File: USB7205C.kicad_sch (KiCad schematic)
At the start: 92 parts, among them CN8 W25Q128FVIQ_Connector, U13 25MHz, U19 LX7167ACLD-TR, U20 USB7205C-I_KDX, U31 USB7206C-I_KDX

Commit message: Initial design of USB7205C
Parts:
- removed C207, C209, C210, C211, C212, C74, C75, C76, C77, C78, C79, C80, C81, C82, C83, C86, C87, C88: 100nF, Capacitor_SMD:C_0402_1005Metric, symbol JLCImport:CL05B104KB54PNC
- removed C67, C73: 15pF, Capacitor_SMD:C_0402_1005Metric, symbol JLCImport:0402CG150J500NT
- removed C84: 10uF, Capacitor_SMD:C_0805_2012Metric, symbol JLCImport:CL21A106KAYNNNE
- removed R189, R60: 200k, Resistor_SMD:R_0603_1608Metric, symbol JLCImport:0603WAF2003T5E
- removed R190, R191, R192, R193, R204, R205, R206, R207, R55, R59: 10k, Resistor_SMD:R_0402_1005Metric, symbol JLCImport:0402WGF1002TCE
- removed R217, R218, R219, R220, R221, R222, R223: 100k, Resistor_SMD:R_0402_1005Metric, symbol JLCImport:0402WGF1003TCE
- removed R376, R394: 100k, Resistor_SMD:R_0402_1005Metric, symbol JLCImport:HP02WAF1003TCE
- removed R54: 12k±1%, Resistor_SMD:R_0402_1005Metric, symbol JLCImport:CR0402F12K0Q10Z
- removed TP2: A, TestPoint:TestPoint_Pad_1.0x1.0mm, symbol Connector:TestPoint
- removed U13: 25MHz, JLCImport:25M_10PF_50PPM, symbol JLCImport:25M_10PF_50PPM
- removed U31: USB7206C-I_KDX, JLCImport:USB7206C-I_KDX, symbol JLCImport:USB7206C-I_KDX
- added C199, C214: 15pF, Capacitor_SMD:C_0402_1005Metric, symbol JLCImport:0402CG150J500NT
- added C216, C217, C218, C219, C221, C222, C304, C321, C322, C323, C324, C325, C326, C327, C328, C329, C330: 100nF, Capacitor_SMD:C_0402_1005Metric, symbol JLCImport:CL05B104KB54PNC
- added C86: 10uF, Capacitor_SMD:C_0805_2012Metric, symbol JLCImport:CL21A106KAYNNNE
- added R217: 12k±1%, Resistor_SMD:R_0402_1005Metric, symbol JLCImport:CR0402F12K0Q10Z
- added R376, R394, R397, R398, R399, R400: 10k, Resistor_SMD:R_0402_1005Metric, symbol JLCImport:0402WGF1002TCE
- added R395, R396: 100k, Resistor_SMD:R_0402_1005Metric, symbol JLCImport:0402WGF1003TCE
- added U21: 25MHz, JLCImport:25M_10PF_50PPM, symbol JLCImport:25M_10PF_50PPM
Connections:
- net +1V1 is gone; now on net VCORE: C156.1, C157.2, C158.2, C159.2, C190.2, L1.1, R8.2
- net VDD33 is gone; now on net +3V3: U20.26 (VDD33), U20.43 (VDD33), U20.53 (VDD33), U20.62 (VDD33), U20.67 (VDD33), U20.79 (VDD33), U20.81 (VDD33), U20.82 (VDD33), U20.88 (VDD33), U20.99 (VDD33)
- net +3V3: now also C216.1, C217.1, C218.1, C219.1, C221.1, C222.1, C304.1, C321.1, R376.2, R394.2, R397.2, R398.2, R399.2, R400.2
- net D+: now also U20.89 (USB2UP_DP)
- net D-: now also U20.90 (USB2UP_DM)
- net GND: now also R216.1, U20.101 (VSS), U20.24 (TESTEN), C199.1, C214.1, C216.2, C217.2, C218.2, C219.2, C221.2, C222.2, C304.2, C321.2, C322.2, C323.2, C324.2, C325.2, C326.2, C327.2, C328.2, C329.2, C330.2, C86.1, R217.1, R395.1, R396.1
- net MI2C_CLK: now also U20.61 (PF18/MSTR_I2C_CLK)
- net MI2C_DATA: now also U20.3 (PF31/MSTR_I2C_DATA)
- net P1_USB2.0_D+: now also U20.5 (USB2DN_DP1/PRT_DIS_P1)
- net P1_USB2.0_D-: now also U20.6 (USB2DN_DM1/PRT_DIS_M1)
- net P1_USB3.0_RX+: now also U20.10 (USB3DN_RXDP1)
- net P1_USB3.0_RX-: now also U20.11 (USB3DN_RXDM1)
- net P1_USB3.0_TX+: now also U20.7 (USB3DN_TXDP1)
- net P1_USB3.0_TX-: now also U20.8 (USB3DN_TXDM1)
- net P2_USB2.0_D+: now also U20.14 (USB2DN_DP2/PRT_DIS_P2)
- net P2_USB2.0_D-: now also U20.15 (USB2DN_DM2/PRT_DIS_M2)
- net P2_USB3.0_RX+: now also U20.19 (USB3DN_RXDP2)
- net P2_USB3.0_RX-: now also U20.20 (USB3DN_RXDM2)
- net P2_USB3.0_TX+: now also U20.16 (USB3DN_TXDP2)
- net P2_USB3.0_TX-: now also U20.17 (USB3DN_TXDM2)
- net P3_USB2.0_D+: now also U20.27 (USB2DN_DP3/PRT_DIS_P3)
- net P3_USB2.0_D-: now also U20.28 (USB2DN_DM3/PRT_DIS_M3)
- net P5_USB2.0_D+: now also U20.42 (USB2DN_DP5/PRT_DIS_P5)
- net P5_USB2.0_D-: now also U20.41 (USB2DN_DM5/PRT_DIS_M5)
- net PRT_CTL5: now also U20.77 (PF28)
- net SSRX+: now also U20.94 (USB3UP_RXDP)
- net SSRX-: now also U20.95 (USB3UP_RXDM)
- net SSTX+: now also U20.91 (USB3UP_TXDP)
- net SSTX-: now also U20.92 (USB3UP_TXDM)
- net VCORE: now also C322.1, C323.1, C324.1, C325.1, C326.1, C327.1, C328.1, C329.1, C330.1, C86.2
- net at U20.100 (RBIAS): now also R217.2
- net at U20.2 (PF30/VBUS_DET): now also R209.2
- net at U20.32 (USB3DN_RXDP3): now also R210.2
- net at U20.33 (USB3DN_RXDM3): now also R211.2
- net P4_USB2.0_D+: now reaches U20.34 (USB2DN_DP4/PRT_DIS_P4)
- net P4_USB2.0_D-: now reaches U20.35 (USB2DN_DM4/PRT_DIS_M4)
- net at U20.39 (USB3DN_RXDP4): now also R395.2
- net at U20.40 (USB3DN_RXDM4): now also R396.2
- net PRT_CTL4: now reaches U20.57 (PF14/PRT_CTL4)
- net at U20.58 (PF15/PRT_CTL3): now also R398.1
- net at U20.59 (PF16/PRT_CTL2): now also R399.1
- net at U20.60 (PF17/PRT_CTL1): now also R400.1
- net at U20.63 (TEST1): now also R376.1
- net at U20.64 (TEST2): now also R394.1
- net at U20.65 (TEST3): now also R397.1
- net at U20.68 (PF21/SPI_CLK): now also R216.2
- net at U20.71 (PF23/SPI_D1): now also R213.2
- net at U20.72 (PF24/SPI_D2): now also R214.2
- net at U20.73 (PF25/SPI_D3): now also R215.2
- net at U20.74 (PF29/GPIO93): now also R212.2
- net at U20.97 (XTALO): now also C199.2, U21.1
- net at U20.98 (XTALI/CLK_IN): now also C214.2, U21.2
- no-connect marks 16 -> 12
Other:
- note added: "Float to disable PortSplit on ports 3 and 4"
- note added: "Weak pull down on SPI_CLK to disable battery charging on all ports"
- note added: "Weak pull down on SPI_D[3:1] to disable battery charging on all ports"
- note added: "Weak pull down to GND to disable GPIO93"
- note removed: "Audio; unused here"
- note removed: "Float to disable PortSplit on ports 3,4,5"
- note removed: "GPIO93 (unused)"
- note removed: "I2S_LRCK"
- note removed: "I2S_MCLK"
- note removed: "I2S_SCK"
- note removed: "I2S_SDI"
- note removed: "I2S_SDO"
- note removed: "MIC_DET"
- note removed: "Master I2C interface unused - weak pull down to disable pin"
- note removed: "NC"
- note removed: "PRT_CTL5_U3"
- note removed: "Tie RESET_N to high permanently to ensure it stays on always"
- moved on the sheet: C195, R200, R201, R202, R203, R344, R352, R360, R368, R384, R385, R390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

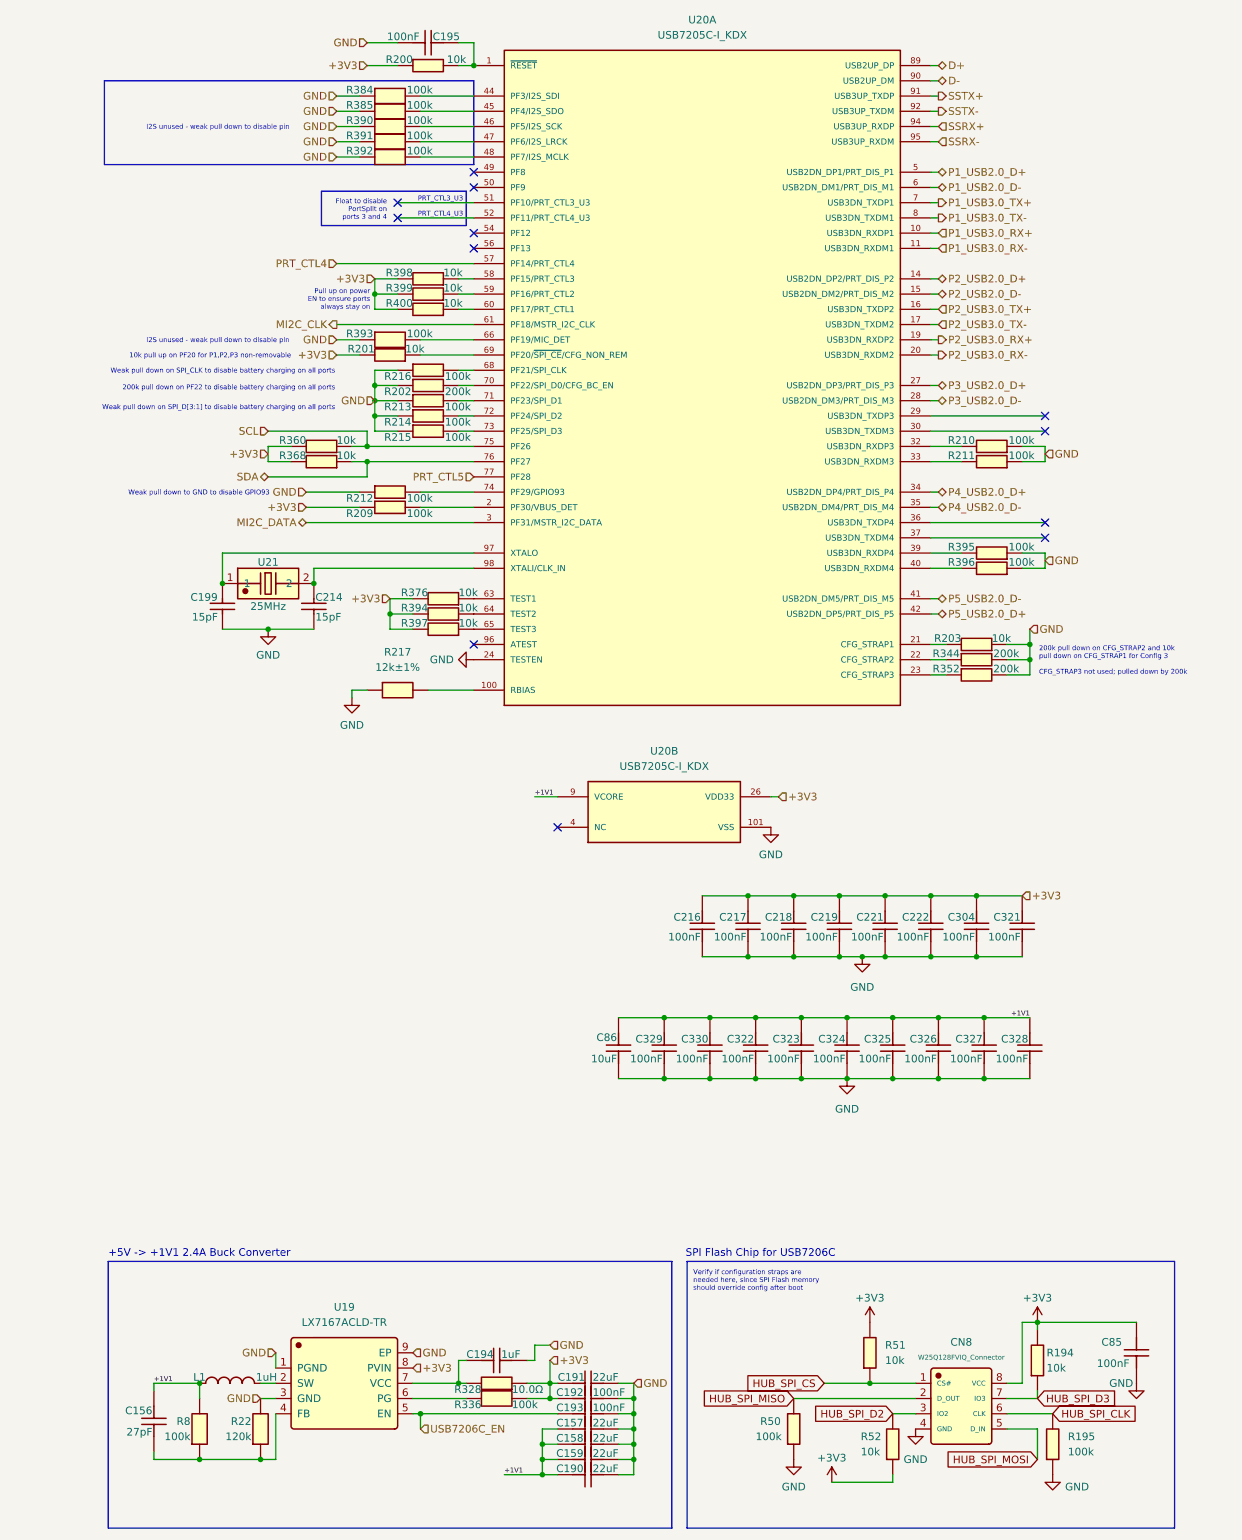
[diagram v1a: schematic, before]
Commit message: Removed SPI flash from USB7205C
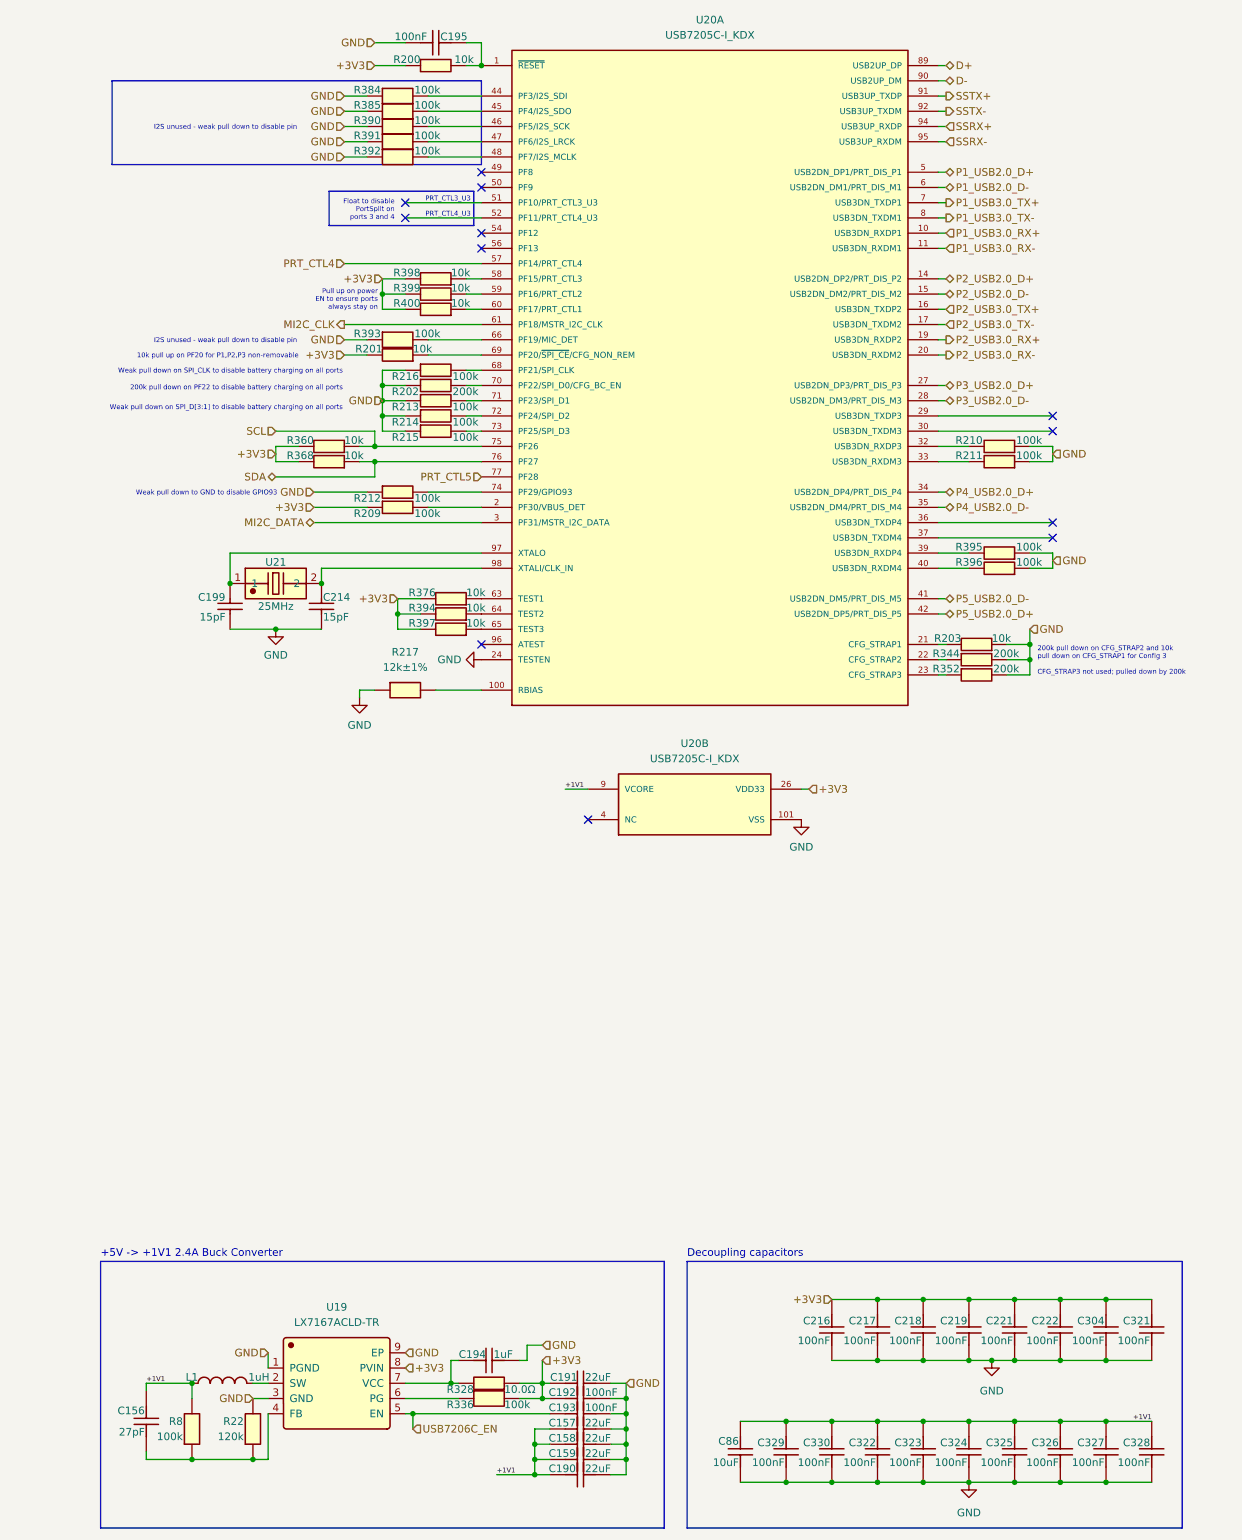
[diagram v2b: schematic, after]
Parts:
- removed C85: 100nF, Capacitor_SMD:C_0402_1005Metric, symbol JLCImport:CL05B104KB54PNC
- removed CN8: W25Q128FVIQ_Connector, JLCImport:H2541FV-C762-2X04P, symbol JLCImport:H2541FV-C762-2X04P
- removed R194, R51, R52: 10k, Resistor_SMD:R_0402_1005Metric, symbol JLCImport:0402WGF1002TCE
- removed R195, R50: 100k, Resistor_SMD:R_0402_1005Metric, symbol JLCImport:0402WGF1003TCE
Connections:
- net +3V3 renamed VDD33
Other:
- note added: "Decoupling capacitors"
- note removed: "SPI Flash Chip for USB7206C"
- note removed: "Verify if configuration straps are needed here, since SPI Flash memory should override config after boot"
- moved on the sheet: C156, C157, C158, C159, C190, C191, C192, C193, C194, C195, C199, C214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

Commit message: Changed VCORE voltage of USB7205C to 1.15V
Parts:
- removed R8: 100k, Resistor_SMD:R_0402_1005Metric, symbol JLCImport:HP02WAF1003TCE
- added R50: 110k, Resistor_SMD:R_0402_1005Metric, symbol JLCImport:HRC0402F1103DNTO
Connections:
- net VCORE: now also R50.2
- net at C156.2, R22.1, U19.4 (FB): now also R50.1
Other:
- note added: "+3V3 -> +1V15 2.4A Buck Converter"
- note removed: "+5V -> +1V1 2.4A Buck Converter"
- moved on the sheet: C156

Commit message: Basic Function Review/Documentation of USB7205C
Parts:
- added R401, R402: 10k, Resistor_SMD:R_0402_1005Metric, symbol JLCImport:0402WGF1002TCE
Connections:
- net USB7206C_EN is gone; now on net VDD33: C193.1, U19.5 (EN)
- net MI2C_CLK: now also R398.1
- net MI2C_DATA: now also R401.1
- net VDD33: now also R401.2, R402.2
- net at U20.58 (PF15/PRT_CTL3): now also R402.1; no longer R398.1
- net SCL renamed SI2C_SCL
- net SDA renamed SI2C_SDA
